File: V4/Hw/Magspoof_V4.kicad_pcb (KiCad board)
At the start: 2 copper layers, 39.5 x 21.9 mm, 50 parts, among them J1 Coil, J2 SWD, P1 USB_C_Plug_USB2.0, Q1 DMG3415U-7, SW1 ON, SW3 S1, SW4 SOURCE MAG, SW5 RESET, U1 CH552G, U2 AP2112K-3.3, U3 TC4424, U5 MCP73831

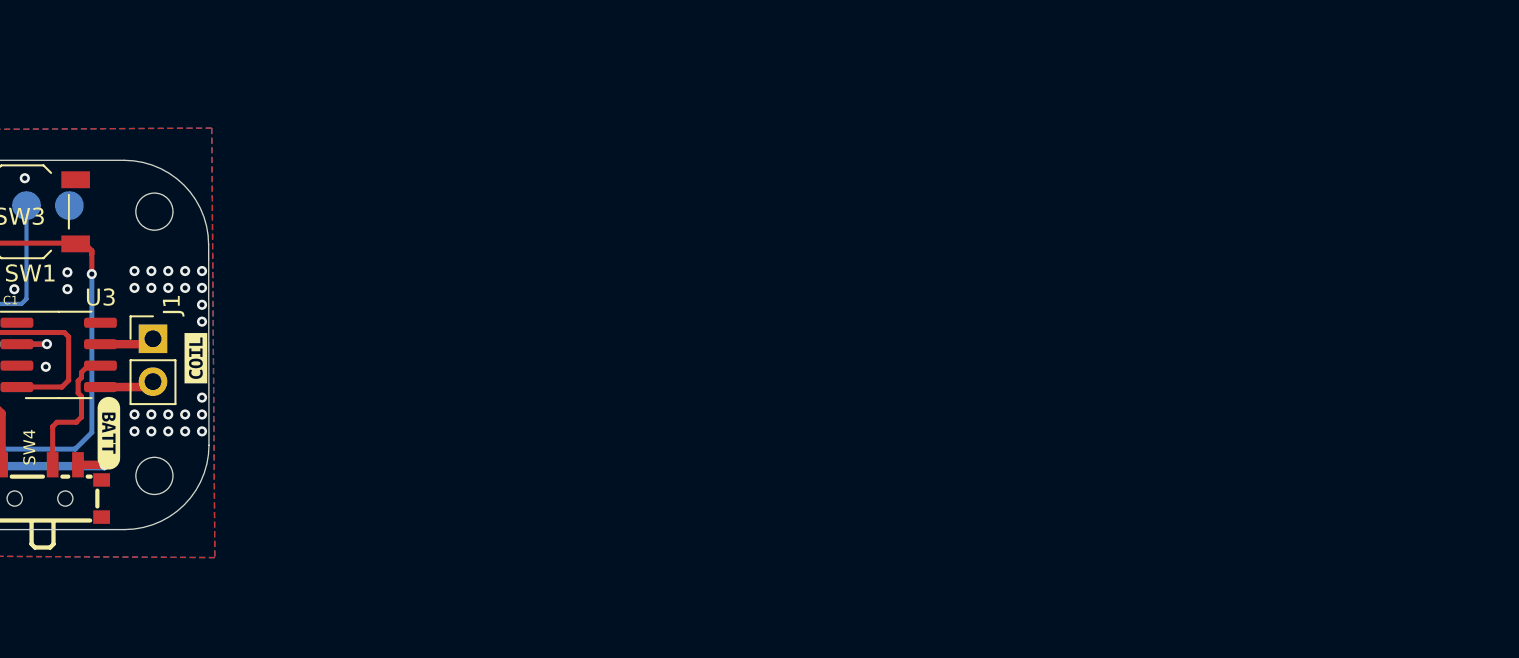
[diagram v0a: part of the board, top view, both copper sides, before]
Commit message: feat: flat spiral coil proposals for PCB antenna
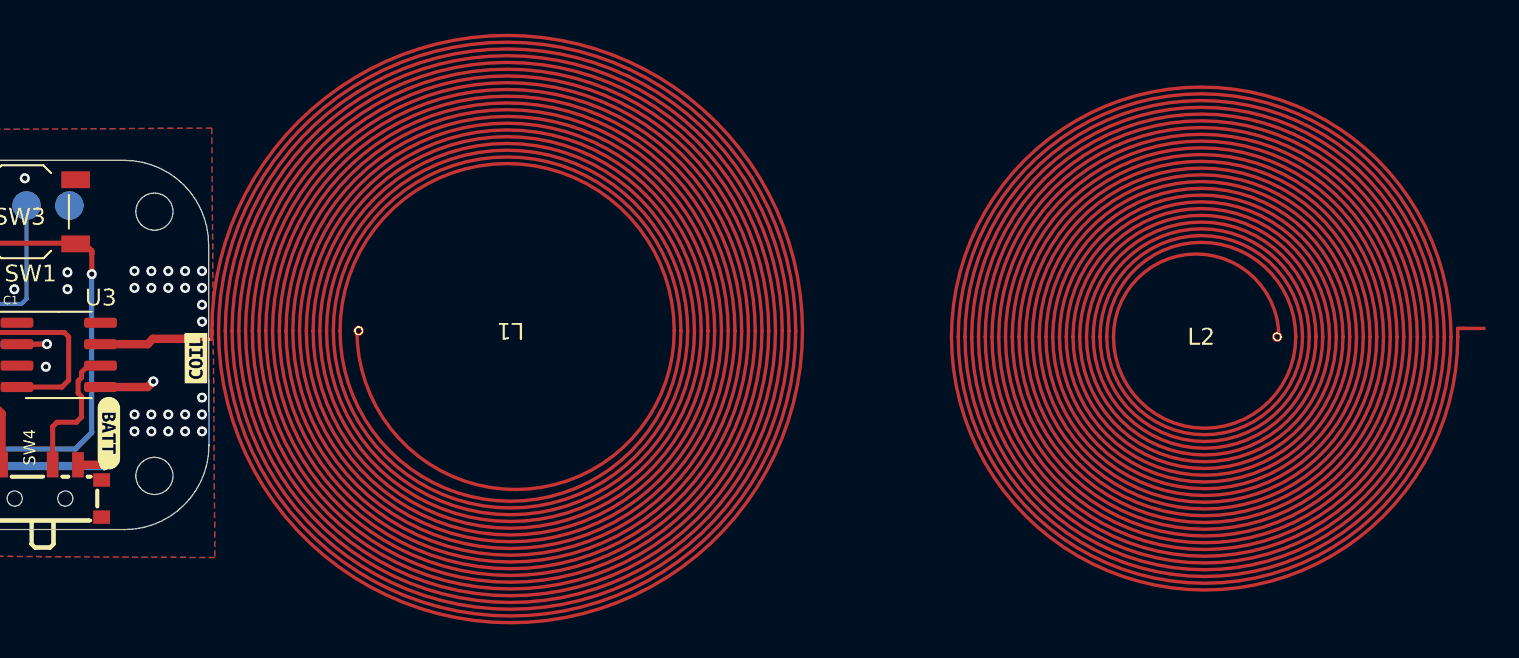
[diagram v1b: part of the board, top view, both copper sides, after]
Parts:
- removed J1: Coil, Connector_PinHeader_2.54mm:PinHeader_1x02_P2.54mm_Vertical
- added L1: ~, Library:Coil_20t_35mm_0.2_0.2_0.6_0.3, F.Cu at (154.3, 56.5)
- added L2: ~, magspoof:Coil_25t_30mm_0.2_0.2_0.6_0.3, F.Cu at (195.2, 56.9)
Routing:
- net /Out_A: track 3.25 -> 5.70 mm
- net /Out_B: track 2.95 -> 3.00 mm, vias 0 -> 1

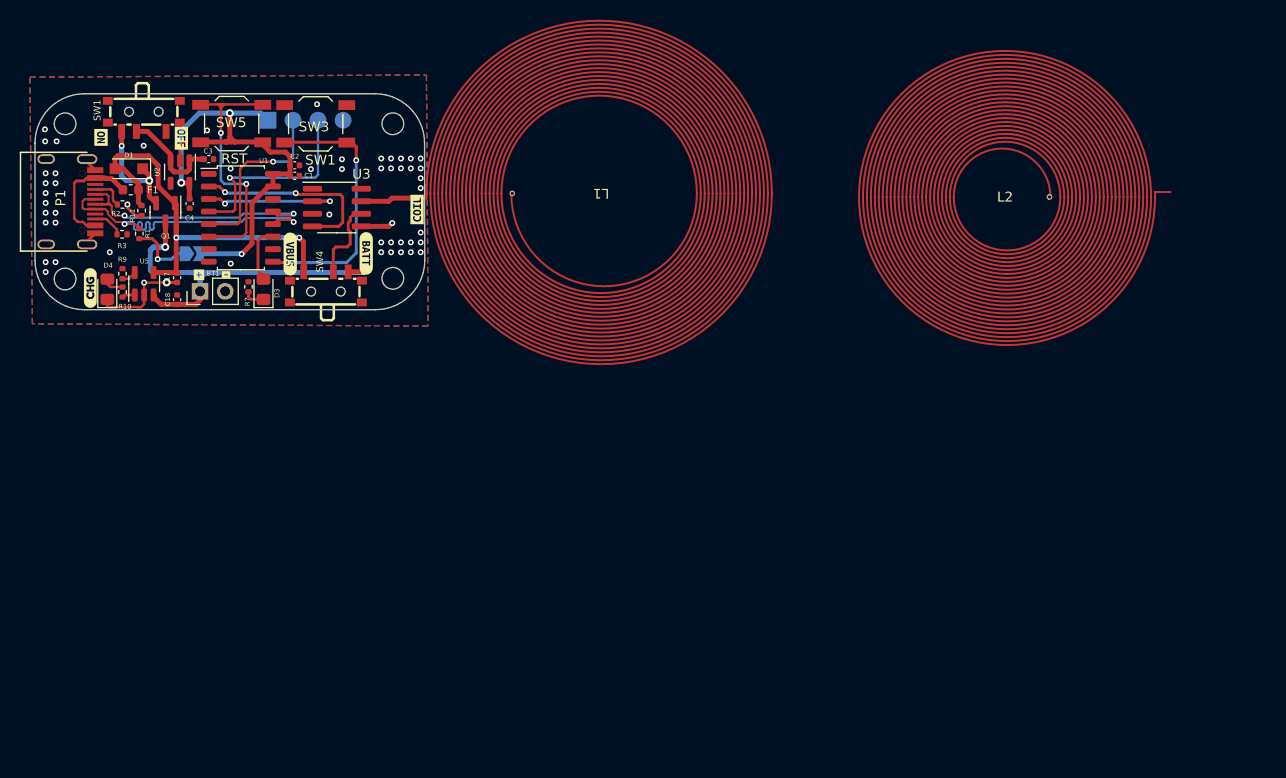
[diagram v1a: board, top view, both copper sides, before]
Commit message: feat(hw): add 2 additional coils and the specs of the coils
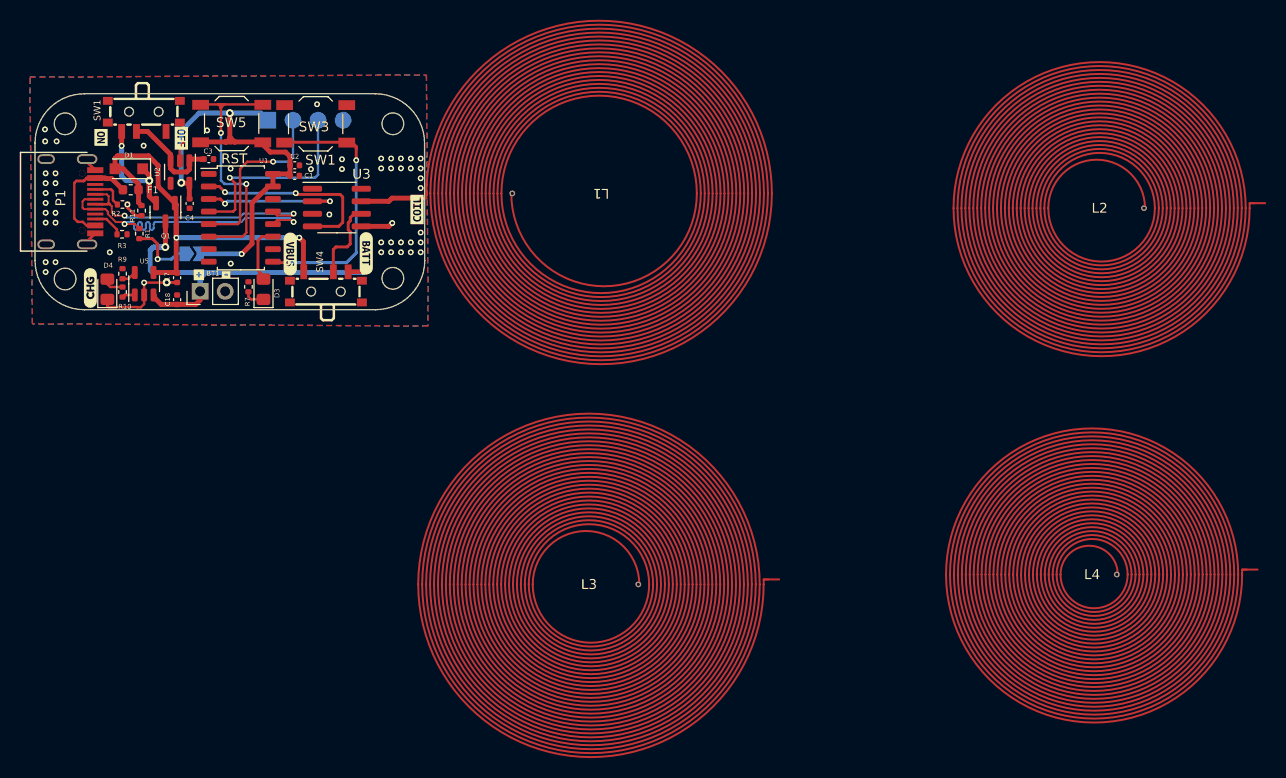
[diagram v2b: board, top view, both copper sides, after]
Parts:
- added L3: 30t_35mm, magspoof:Coil_30t_35mm_0.2_0.2_0.6_0.3, F.Cu at (153.1, 96.2)
- added L4: 30t_30mm, magspoof:Coil_30t_30mm_0.2_0.2_0.6_0.3, F.Cu at (204.0, 95.2)
- L1: value ~ -> 20t_35mm
- L2: value ~ -> 25t_30mm
- moved L2 9.65 mm to (204.8, 58.0)
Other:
- board text added: "N=20 Dout=35mm R=9 L=14.8uH"
- board text added: "N=25 Dout=30mm R=9.6 L=13.2uH"
- board text added: "N=30 Dout=30mm R=11.52 L=14.18uH"
- board text added: "N=30 Dout=35mm R=13.46 L=21.2uH"
- board text added: "PCB tickness = 0.8 mm"
